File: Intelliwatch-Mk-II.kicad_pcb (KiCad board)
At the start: 4 copper layers, 123.7 x 100 mm, 75 parts, among them J1 Voltmeter Probes, J2 DC Power Input, J3 USB_C_Receptacle_USB2.0_16P, J4 Flashlight Terminals, J5 CONN LCD 1.8 TFT SPI, J6 Conn 7S-4D HW-069 I2C, Q1 NDS331N, SW1 PWR SPST, SW2 EN Button, SW3 LCD LED SPST, SW4 Cherry MX Keyswitch, SW5 Cherry MX Keyswitch, SW6 Cherry MX Keyswitch, SW7 Cherry MX Keyswitch, SW8 PROG Button, U1 SN74HC02N, U2 MCP3421A0T-ECH, U3 74AHC1G04GW_125, U4 74AHC1G04GW_125, U5 LM7805, U6 CH340C, U7 SY8120IABC, U8 QMC5883L, U9 ESP32-WROOM-32UE

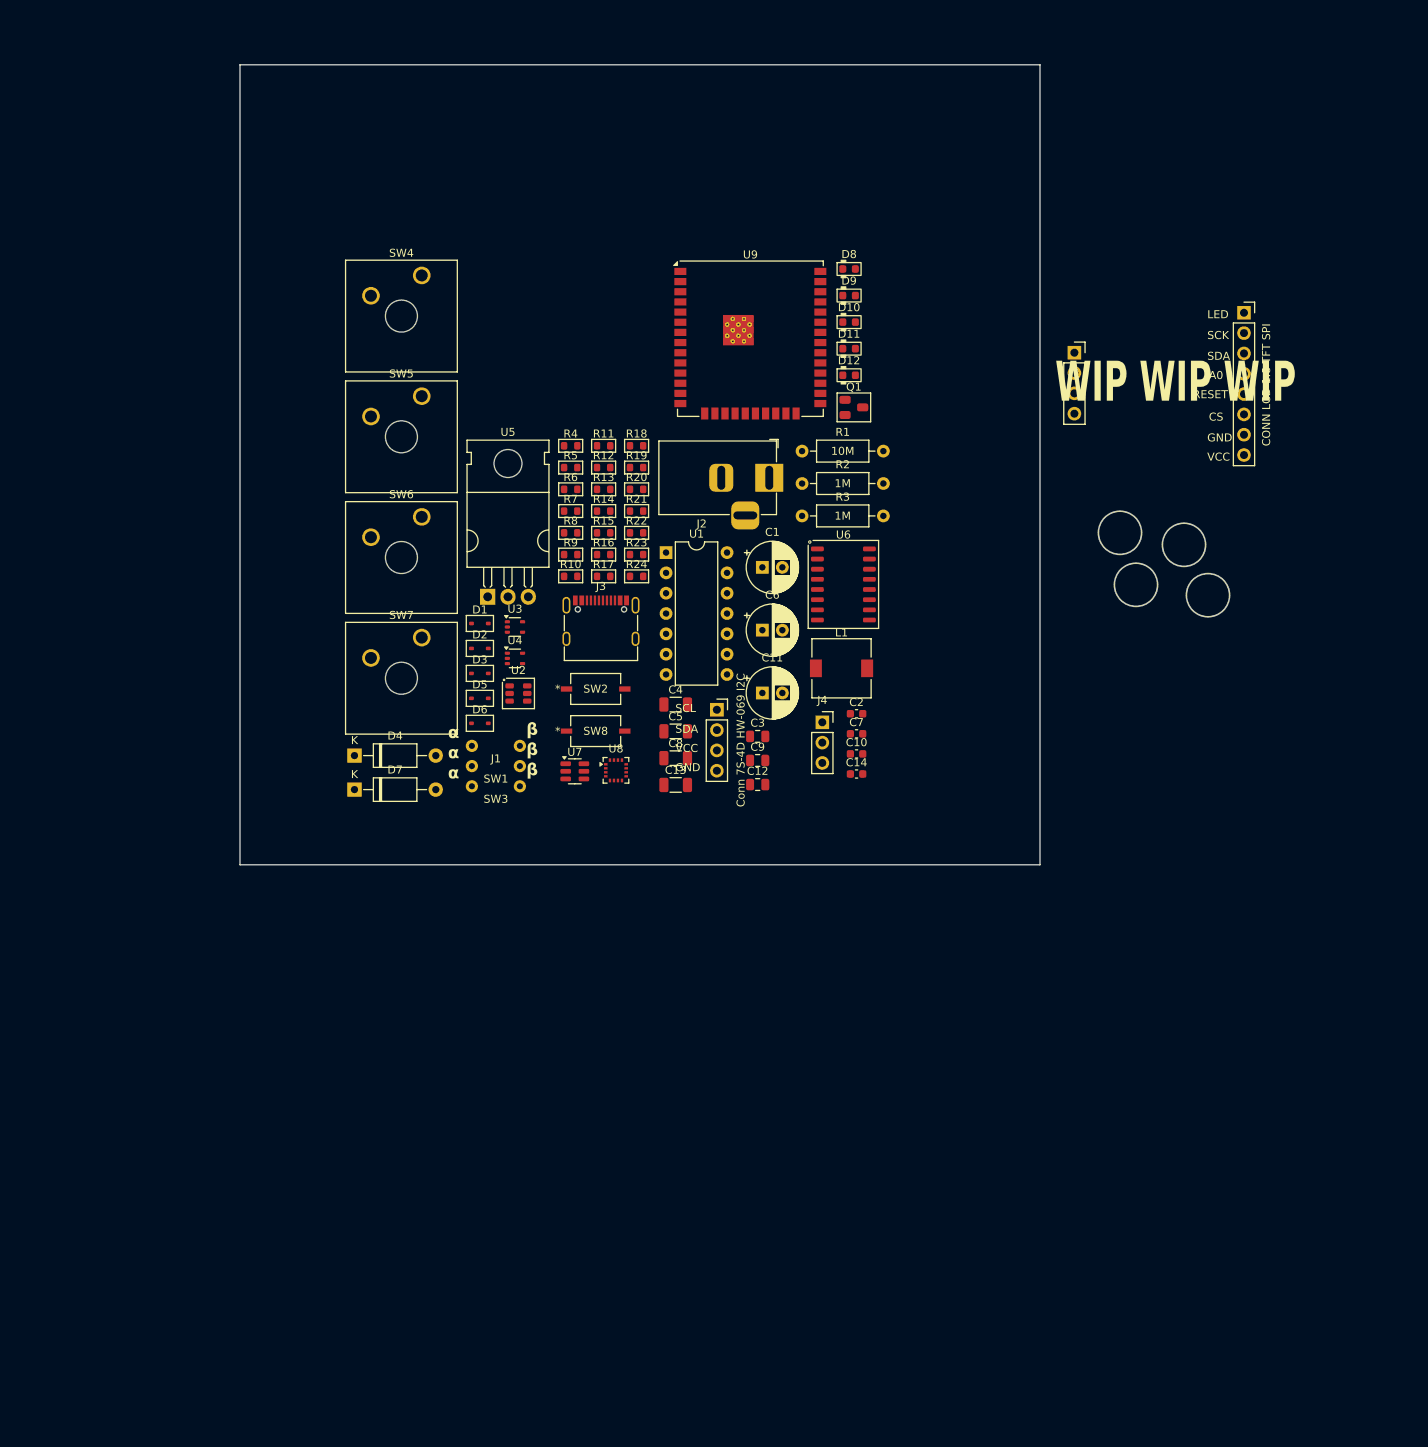
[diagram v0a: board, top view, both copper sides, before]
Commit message: ADDED TFT LCD footprint w/clearance. FIXED trace width and clearance. TODO arrange PCB.
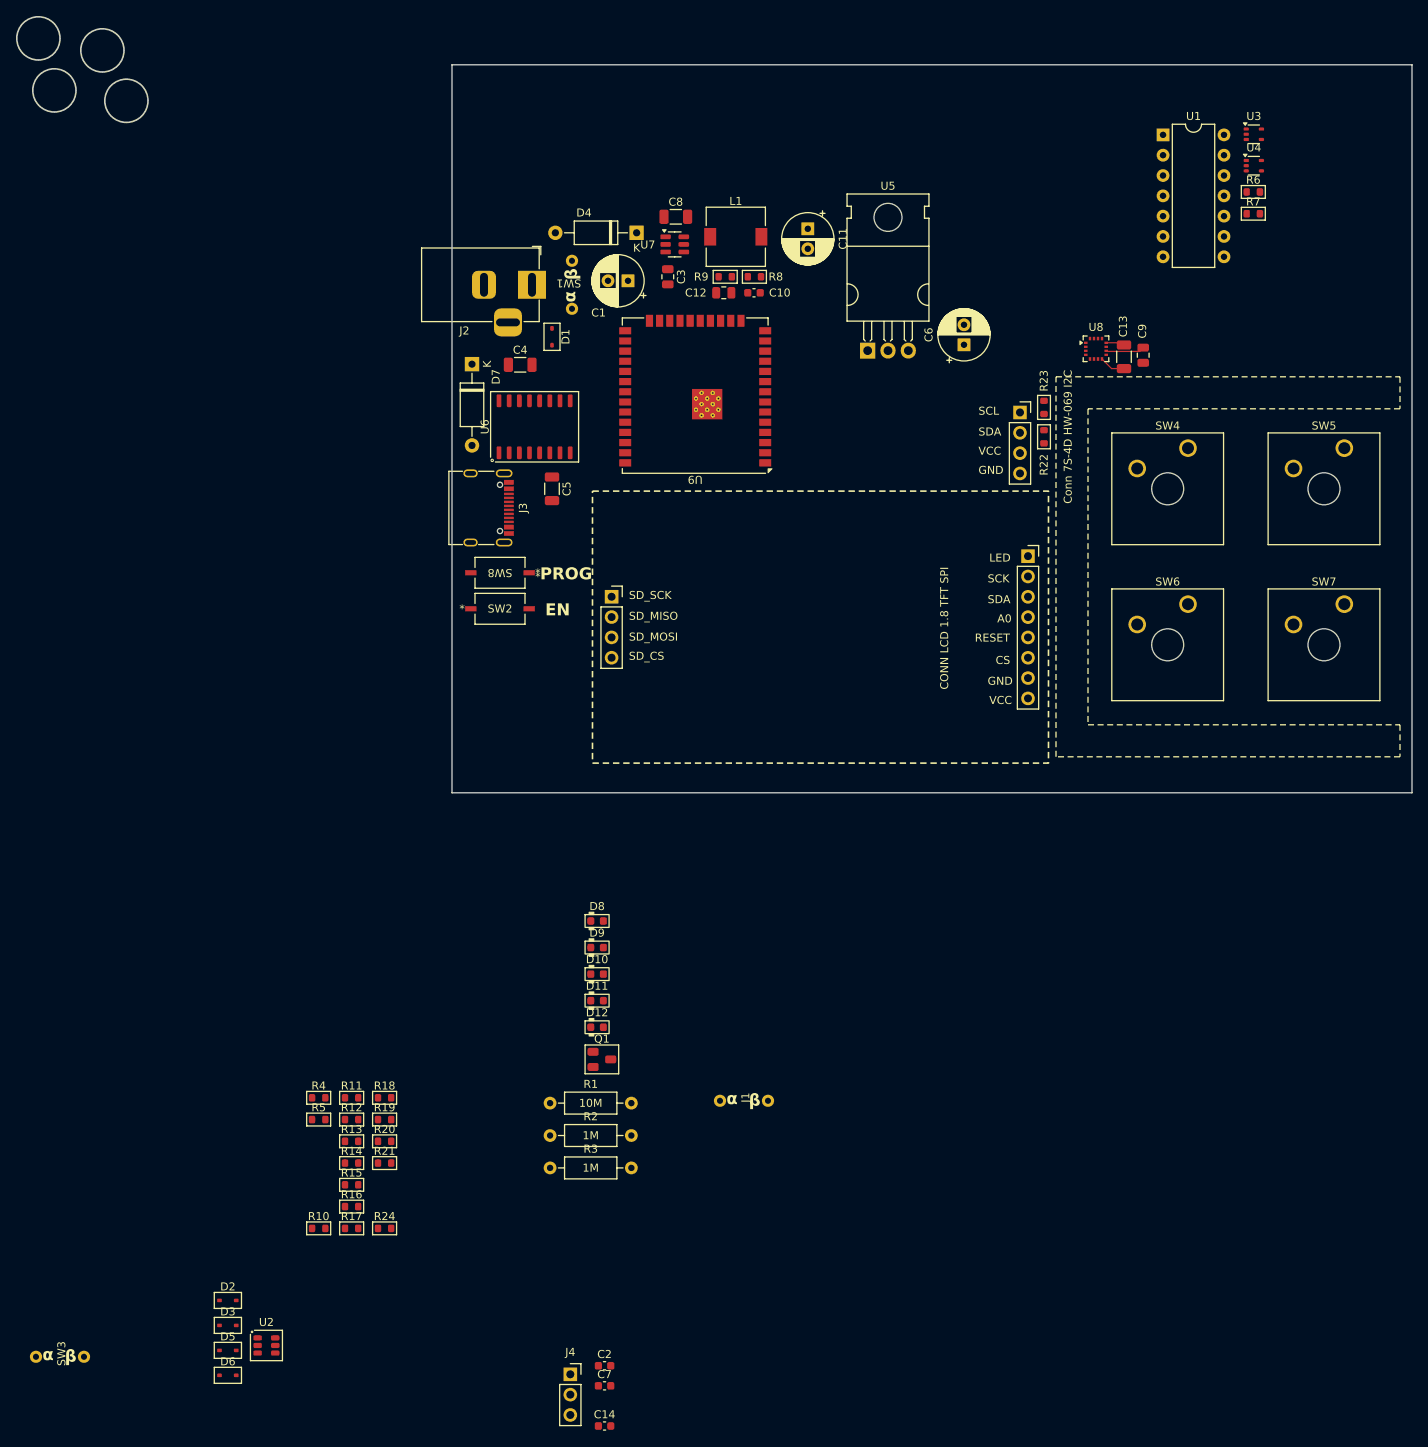
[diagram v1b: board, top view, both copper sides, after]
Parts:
- moved SW5 115.5 mm to (182.5, 69.4)
- moved SW7 115.4 mm to (182.5, 88.9)
- moved U3 111.0 mm to (171.2, 30.2)
- moved U4 111.0 mm to (171.2, 34.1)
- moved SW4 98.2 mm to (163.0, 69.4)
- moved SW6 96.4 mm to (163.0, 88.9)
- moved R6 93.1 mm to (171.2, 37.4)
- moved R7 93.1 mm to (171.2, 40.1)
- moved SW3 89.7 mm to (22.0, 183.0)
- moved D11 87.4 mm to (89.1, 138.5)
- moved D2 87.4 mm to (43.0, 176.0)
- moved U2 87.4 mm to (47.8, 181.6)
- moved C14 87.4 mm to (90.1, 191.7)
- moved C2 87.4 mm to (90.1, 184.1)
- moved C7 87.4 mm to (90.1, 186.6)
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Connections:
- U8 pad 13: Net-(U8-S1) -> +3V3
- U8 pad 4: Net-(U8-S1) -> +3V3
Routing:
- net Net-(U8-C1): track 0.00 -> 4.85 mm
- net Net-(U8-SETP): track 0.00 -> 3.25 mm
- net Net-(U8-SETC): track 0.00 -> 2.34 mm
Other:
- board size 123.7 x 100 mm -> 174.4 x 97 mm
- board text added: "EN"
- board text added: "PROG"

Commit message: FIXED board dimensions to be within minimum to avoid engineering fee. ADDED traces and copper areas for all power/ground nets. TODO is connecting signal lines, and maybe try using that autorouter plugin.
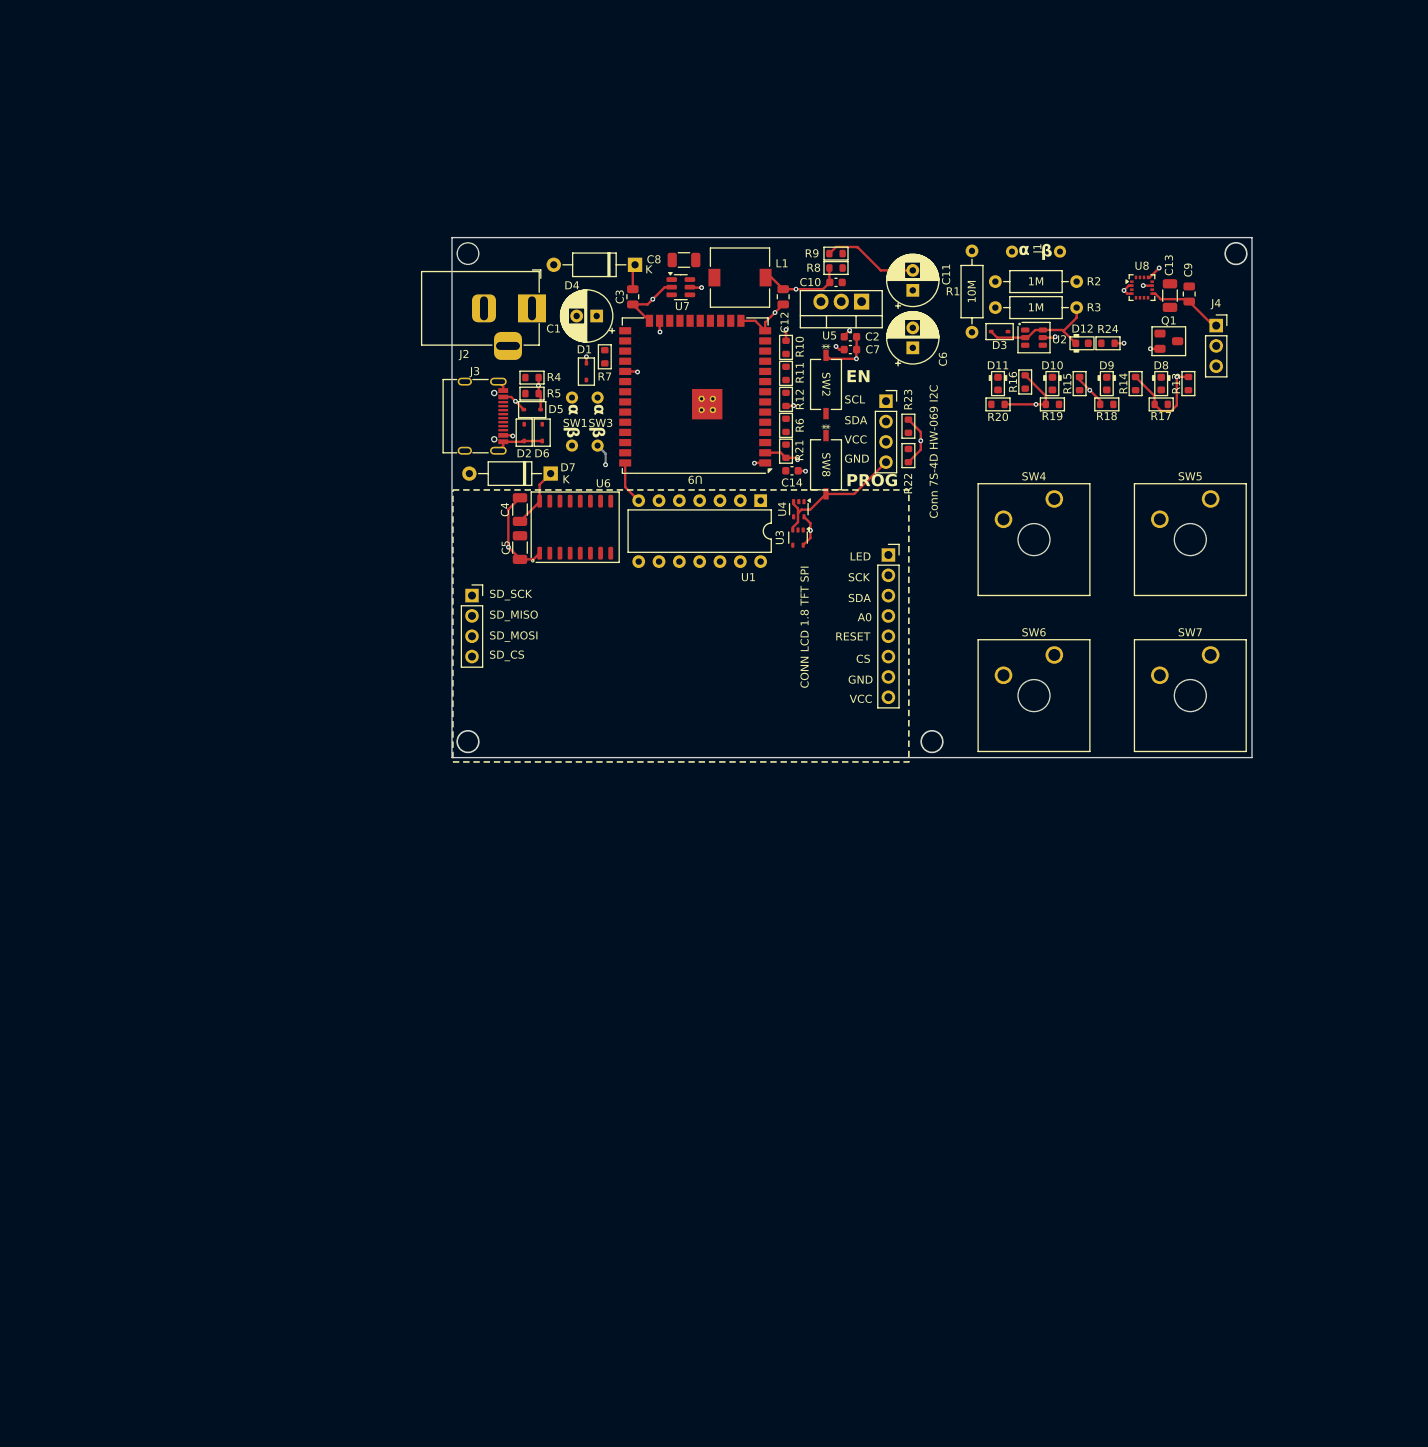
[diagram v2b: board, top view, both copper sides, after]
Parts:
- U5: footprint PCM_Package_TO_SOT_THT_AKL:TO-220-3_Horizontal_TabDown -> PCM_Package_TO_SOT_THT_AKL:TO-220-3_Vertical
- moved U2 158.4 mm to (143.8, 55.6)
- moved D3 157.3 mm to (139.4, 54.9), turned to 180 degrees
- moved J4 154.0 mm to (166.5, 54.1)
- moved R17 144.4 mm to (159.7, 64.0), turned to 180 degrees
- moved R24 142.9 mm to (153.0, 56.3), turned to 180 degrees
- moved R13 141.1 mm to (163.1, 61.4), turned to 90 degrees
- moved R14 138.2 mm to (156.4, 61.4), turned to 90 degrees
- moved R15 135.3 mm to (149.4, 61.4), turned to 90 degrees
- moved SW3 134.8 mm to (89.2, 66.1), turned to -90 degrees
- moved C7 133.1 mm to (120.8, 57.1)
- moved R16 133.1 mm to (142.7, 61.1), turned to 90 degrees
- moved C2 132.2 mm to (120.8, 55.5)
- moved R18 125.1 mm to (152.8, 64.0), turned to 180 degrees
- moved R10 124.7 mm to (112.8, 56.8), turned to -90 degrees
- moved D6 124.2 mm to (82.3, 67.5), turned to -90 degrees
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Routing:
- net +5V: track 0.00 -> 120.4 mm, vias 0 -> 1
- net GND: track 0.00 -> 113.4 mm, vias 0 -> 11
- net +3V3: track 0.00 -> 63.3 mm, vias 0 -> 13
- net +BATT: track 0.00 -> 54.7 mm, vias 0 -> 3
- net Net-(J5-LED): track 0.00 -> 42.8 mm, vias 0 -> 1
- net Net-(D5-K): track 0.00 -> 17.4 mm, vias 0 -> 2
- net Net-(U8-C1): track 4.85 -> 0.00 mm
- net Net-(U8-SETP): track 3.25 -> 0.00 mm
- net Net-(U8-SETC): track 2.34 -> 0.00 mm
- added copper zone on In1.Cu, net +3V3
- added copper zone on In2.Cu, net GND
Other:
- board size 174.4 x 97 mm -> 100 x 65 mm

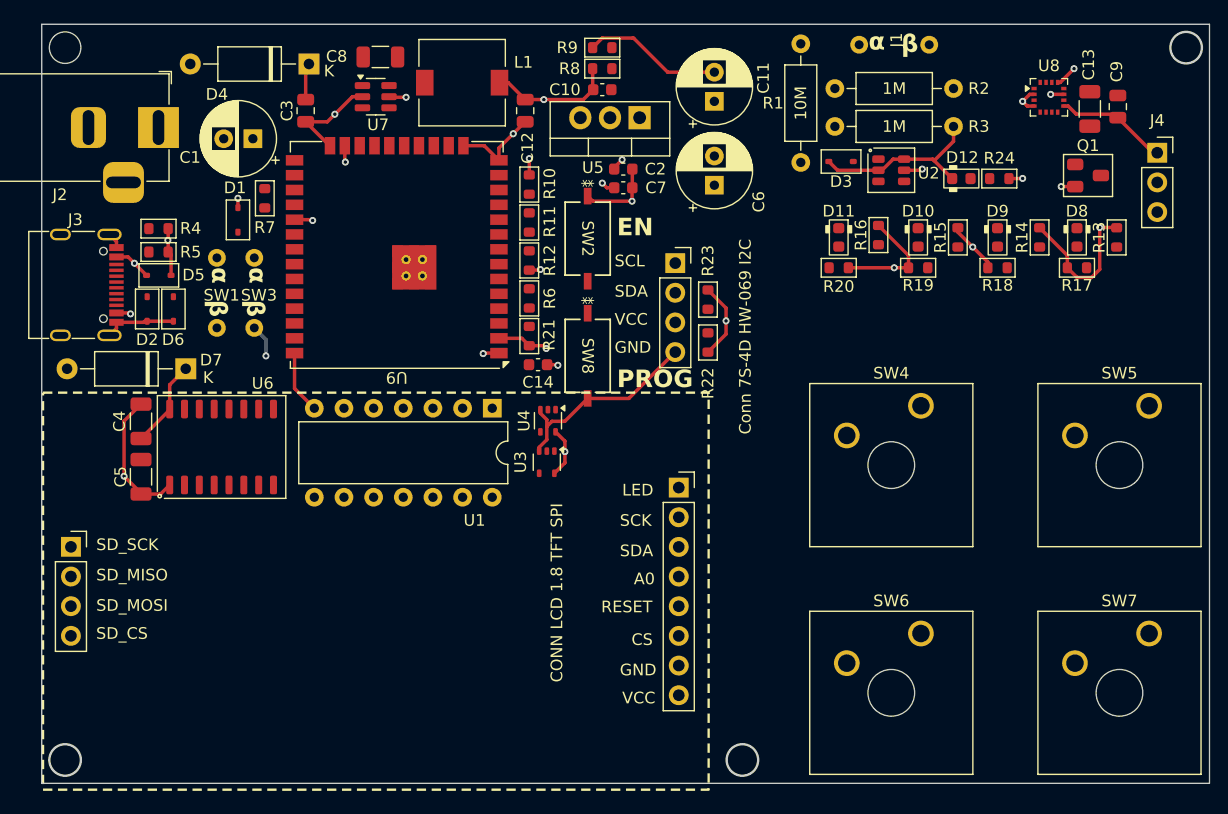
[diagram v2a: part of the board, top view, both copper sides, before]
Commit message: FIXED ESD/TVS diodes to be a different part with practically identical specs.
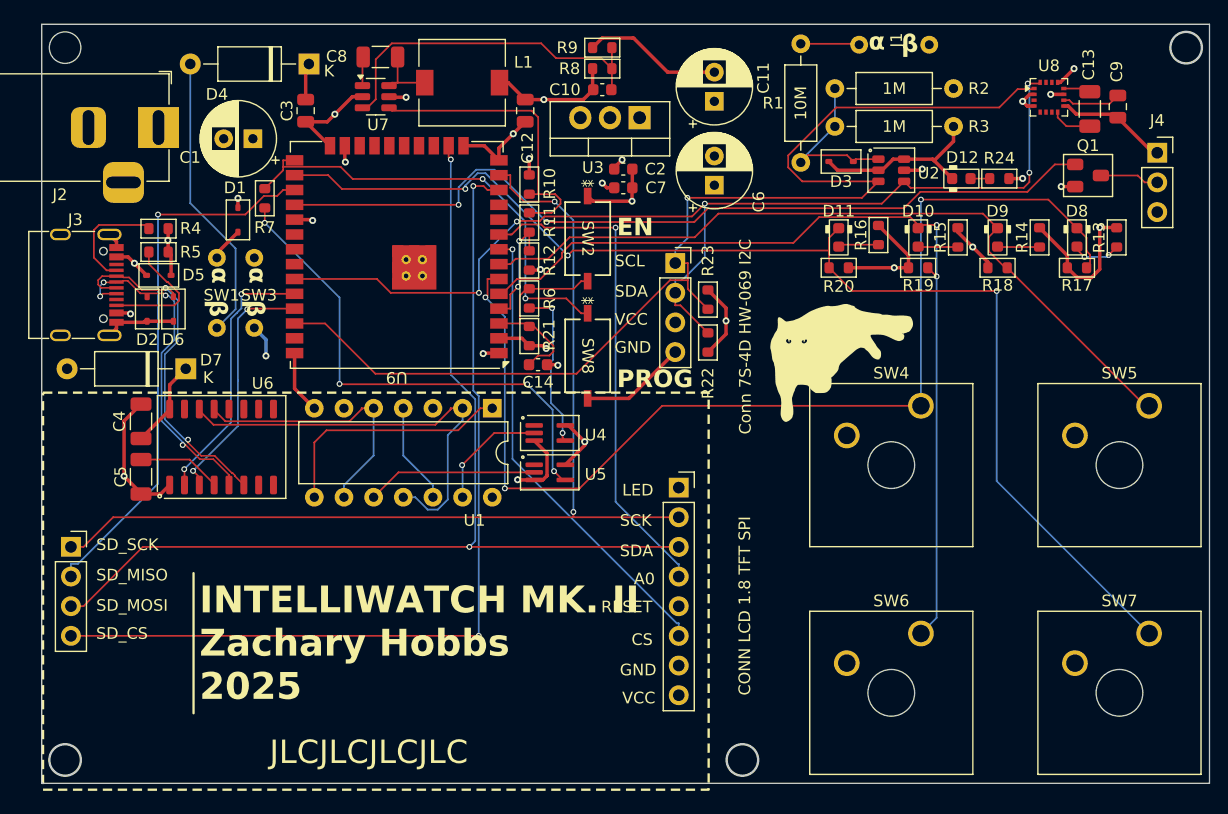
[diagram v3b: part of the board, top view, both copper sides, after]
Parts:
- removed the U3 at (114.2, 80.6)
- added G***: LOGO, ZCustomFootprints:flufftest_3, F.Cu at (135.6, 73.1)
- added U5: 74AHC1G14, PCM_Package_TO_SOT_SMD_AKL:SOT-353_SC-70-5_BigPads, F.Cu at (114.5, 81.5)
- D1, D2, D3, D5, D6: value BV05C -> TVS/ESD
- U4: value 74AHC1G04GW_125 -> 74AHC1G14; footprint Package_TO_SOT_SMD:SOT-353_SC-70-5 -> PCM_Package_TO_SOT_SMD_AKL:SOT-353_SC-70-5_BigPads
- moved U4 1.06 mm to (114.5, 78.1), turned to 0 degrees
- turned R7 to 90 degrees
- renumbered U5 to U3
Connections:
- net Net-(D2-K) renamed /D+
- net Net-(D6-K) renamed /D-
- R6 pad 2: Net-(U3-Y) -> Net-(R6-Pad2)
- R7 pad 1: IO0 -> Net-(R7-Pad1)
- R7 pad 2: Net-(U4-Y) -> IO0
- U1 pad 10: Net-(U4-A) -> Net-(U1-Pad10)
- U1 pad 13: Net-(U3-A) -> Net-(U1-Pad13)
- U4 pad 2: Net-(U4-A) -> Net-(U1-Pad13)
- U4 pad 4: Net-(U4-Y) -> Net-(R6-Pad2)
- U6 pad 2: TX_USB -> RX_USB
- U6 pad 3: RX_USB -> TX_USB
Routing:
- net KEYSW_4: track 0.00 -> 103.7 mm, vias 0 -> 3
- net I2C_SCL: track 0.00 -> 100.2 mm, vias 0 -> 1
- net KEYSW_1: track 0.00 -> 94.2 mm, vias 0 -> 3
- net I2C_SDA: track 0.00 -> 93.0 mm, vias 0 -> 5
- net VSPI_MOSI: track 0.00 -> 89.7 mm, vias 0 -> 2
- net VSPI_SCL: track 0.00 -> 87.1 mm, vias 0 -> 2
- net KEYSW_3: track 0.00 -> 77.6 mm, vias 0 -> 2
- net CS_SD: track 0.00 -> 76.0 mm, vias 0 -> 2
- net FL_MODE: track 0.00 -> 72.9 mm, vias 0 -> 2
- net KEYSW_2: track 0.00 -> 66.5 mm
- net VSPI_MISO: track 0.00 -> 47.0 mm, vias 0 -> 1
- net Net-(R7-Pad1): track 0.00 -> 43.5 mm, vias 0 -> 4
- net TFT_A0_DC: track 0.00 -> 42.6 mm, vias 0 -> 1
- net CS_LCD: track 0.00 -> 40.3 mm, vias 0 -> 1
- net IO0: track 0.00 -> 39.2 mm, vias 0 -> 2
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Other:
- board text added: "INTELLIWATCH MK. II Zachary Hobbs 2025"
- board text added: "JLCJLCJLCJLC"
